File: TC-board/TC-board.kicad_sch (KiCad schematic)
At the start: 7 parts, among them J1 DB15_Female, J3 PCIE-LP-01-01-F-DV-A-TR

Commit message: Updated HX, TC boards.
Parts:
- removed U?: PCF8575_Breakout, symbol PCF8575_Breakout:PCF8575_Breakout
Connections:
- net +3.3V: now also J3.B12, J3.B13
- net GND: now also J3.A11, J3.A14, J3.A3, J3.A7, J3.B11, J3.B14, J3.B8
- net MISO: now also J3.B3
- net SCK: now also J3.B1
- net TC1_CS: now also J3.B9
- net TC2_CS: now also J3.B10
- no-connect marks 22 -> 32
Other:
- note removed: "GPIO Expander"

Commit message: Updated schematics of TC,PT
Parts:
- removed J?: Conn_01x06_Male, symbol Connector:Conn_01x06_Male
- added J3: Conn_01x08_Male, Connector_PinHeader_2.54mm:PinHeader_1x08_P2.54mm_Vertical, symbol Connector:Conn_01x08_Male
- added JP1, JP2, JP3: SolderJumper_3_Open, Jumper:SolderJumper-3_P2.0mm_Open_TrianglePad1.0x1.5mm, symbol Jumper:SolderJumper_3_Open
- added JP4: SolderJumper_2_Open, Jumper:SolderJumper-2_P1.3mm_Open_TrianglePad1.0x1.5mm, symbol Jumper:SolderJumper_2_Open
- added U4: MAX31855KASA, MAX31855_Breakout:MAX31855_Breakout, symbol Sensor_Temperature:MAX31855KASA
- U1, U2, U3: renamed from U?; footprint Package_SO:SOIC-8_3.9x4.9mm_P1.27mm -> MAX31855_Breakout:MAX31855_Breakout
- renumbered J3 to J2
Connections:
- net +3.3V: now also J2.B14, U4.4 (VCC); no longer J2.B12
- net GND: now also J2.A12, J2.A15, J2.A6, J2.B12, J2.B15, J2.B3, U4.1 (GND); no longer J2.A11, J2.A14, J2.A7, J2.B11, J2.B14
- net TC1_CS: now also JP1.1 (A); no longer J2.B9
- net TC1_T+: now also J3.2 (Pin_2)
- net TC1_T-: now also J3.1 (Pin_1)
- net TC2_CS: now also JP2.1 (A); no longer J2.B10
- net TC2_T+: now also J3.4 (Pin_4)
- net TC2_T-: now also J3.3 (Pin_3)
- net TC3_CS: now also JP3.1 (A)
- net TC3_T+: now also J3.6 (Pin_6)
- net TC3_T-: now also J3.5 (Pin_5)
- net SPI1_SCK: now reaches J2.A4
- net SPI1_SCK: now also U1.5 (SCK), U2.5 (SCK), U3.5 (SCK)
- net SPI1_MISO: now reaches J2.A5
- net SPI1_MISO: now also U1.7 (SO), U2.7 (SO), U3.7 (SO)
- net SPI0_MISO: now reaches J2.B2
- net SPI0_MISO: now also U4.7 (SO)
- net TC4_T+: now reaches J1.12 (P12)
- net TC4_T+: now also J3.8 (Pin_8), U4.3 (T+)
- net TC4_T-: now reaches J1.4
- net TC4_T-: now also J3.7 (Pin_7), U4.2 (T-)
- removed net MISO: J2.B3, U1.7 (SO), U2.7 (SO), U3.7 (SO)
- removed net SCK: J2.B1, U1.5 (SCK), U2.5 (SCK), U3.5 (SCK)
- new net CS1: J2.B9, JP1.2 (C)
- new net CS2: J2.B10, JP2.2 (C)
- new net CS3: J2.B11, JP3.2 (C)
- new net CS4: J2.A11, JP4.2 (B)
- new net SPI0_SCK: J2.B1, U4.5 (SCK)
- new net TC4_CS: JP1.3 (B), JP2.3 (B), JP3.3 (B), JP4.1 (A), U4.6 (~{CS})
- no-connect marks 32 -> 25
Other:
- moved on the sheet: U1, U2, U3

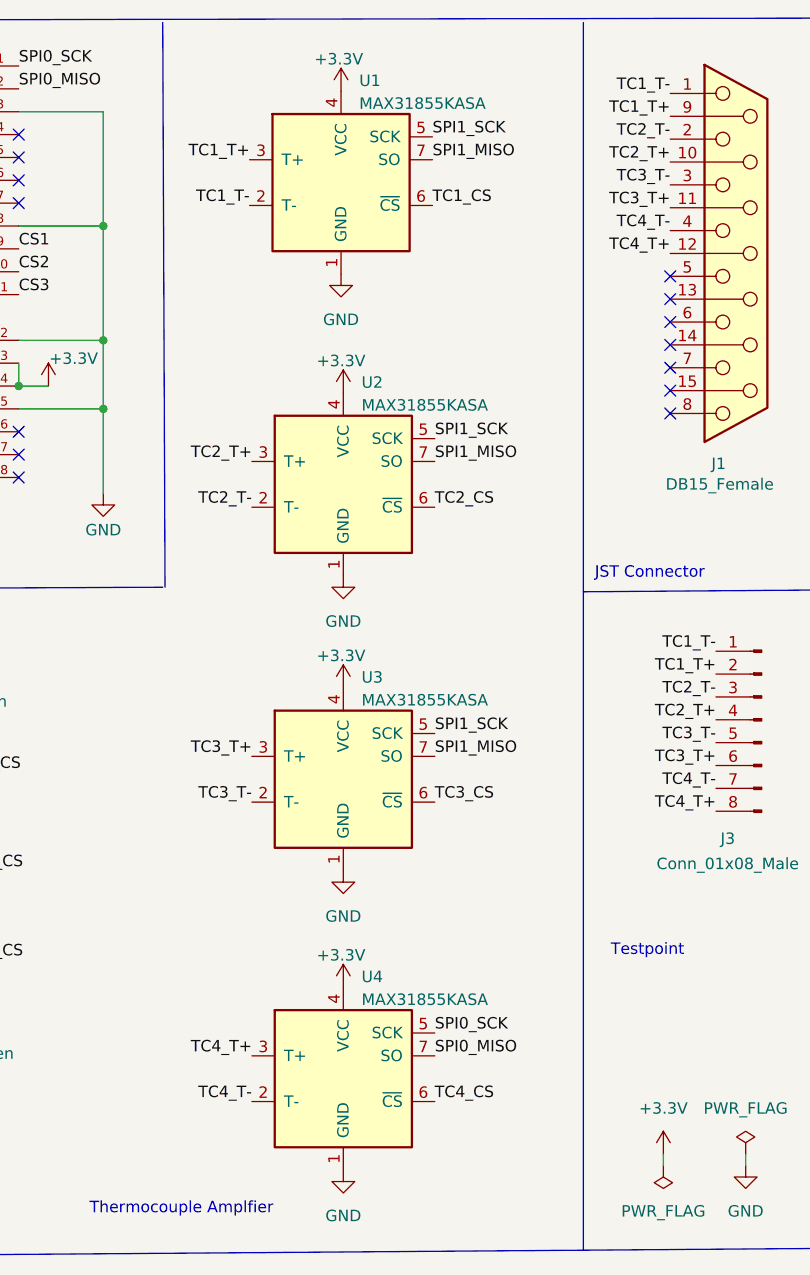
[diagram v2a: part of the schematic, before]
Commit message: Replaced mosfet board with Conor's design using BTS3080EJXUMA1. Modified max31855 symbol to have A (separate assembly) reference designator.
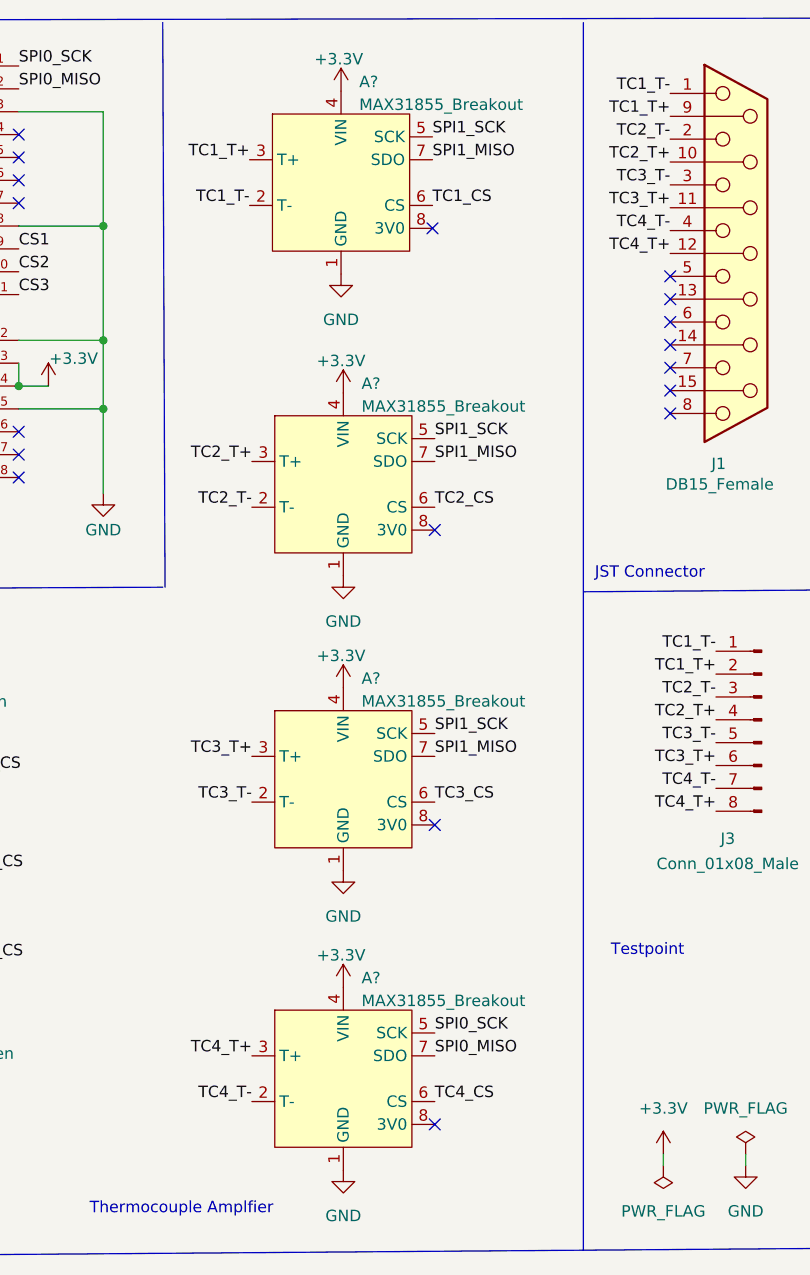
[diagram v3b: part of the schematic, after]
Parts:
- removed U1, U2, U3, U4: MAX31855KASA, MAX31855_Breakout:MAX31855_Breakout, symbol Sensor_Temperature:MAX31855KASA
- added A? (x4): MAX31855_Breakout, symbol MAX31855_Breakout:MAX31855_Breakout
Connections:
- net +3.3V: now also A?.4 (VIN), A?.4 (VIN), A?.4 (VIN), A?.4 (VIN)
- net GND: now also A?.1 (GND), A?.1 (GND), A?.1 (GND), A?.1 (GND)
- net SPI0_MISO: now also A?.7 (SDO)
- net SPI0_SCK: now also A?.5 (SCK)
- net SPI1_MISO: now also A?.7 (SDO), A?.7 (SDO), A?.7 (SDO)
- net SPI1_SCK: now also A?.5 (SCK), A?.5 (SCK), A?.5 (SCK)
- net TC1_CS: now also A?.6 (CS)
- net TC1_T+: now also A?.3 (T+)
- net TC1_T-: now also A?.2 (T-)
- net TC2_CS: now also A?.6 (CS)
- net TC2_T+: now also A?.3 (T+)
- net TC2_T-: now also A?.2 (T-)
- net TC3_CS: now also A?.6 (CS)
- net TC3_T+: now also A?.3 (T+)
- net TC3_T-: now also A?.2 (T-)
- net TC4_CS: now also A?.6 (CS)
- net TC4_T+: now also A?.3 (T+)
- net TC4_T-: now also A?.2 (T-)
- no-connect marks 25 -> 29

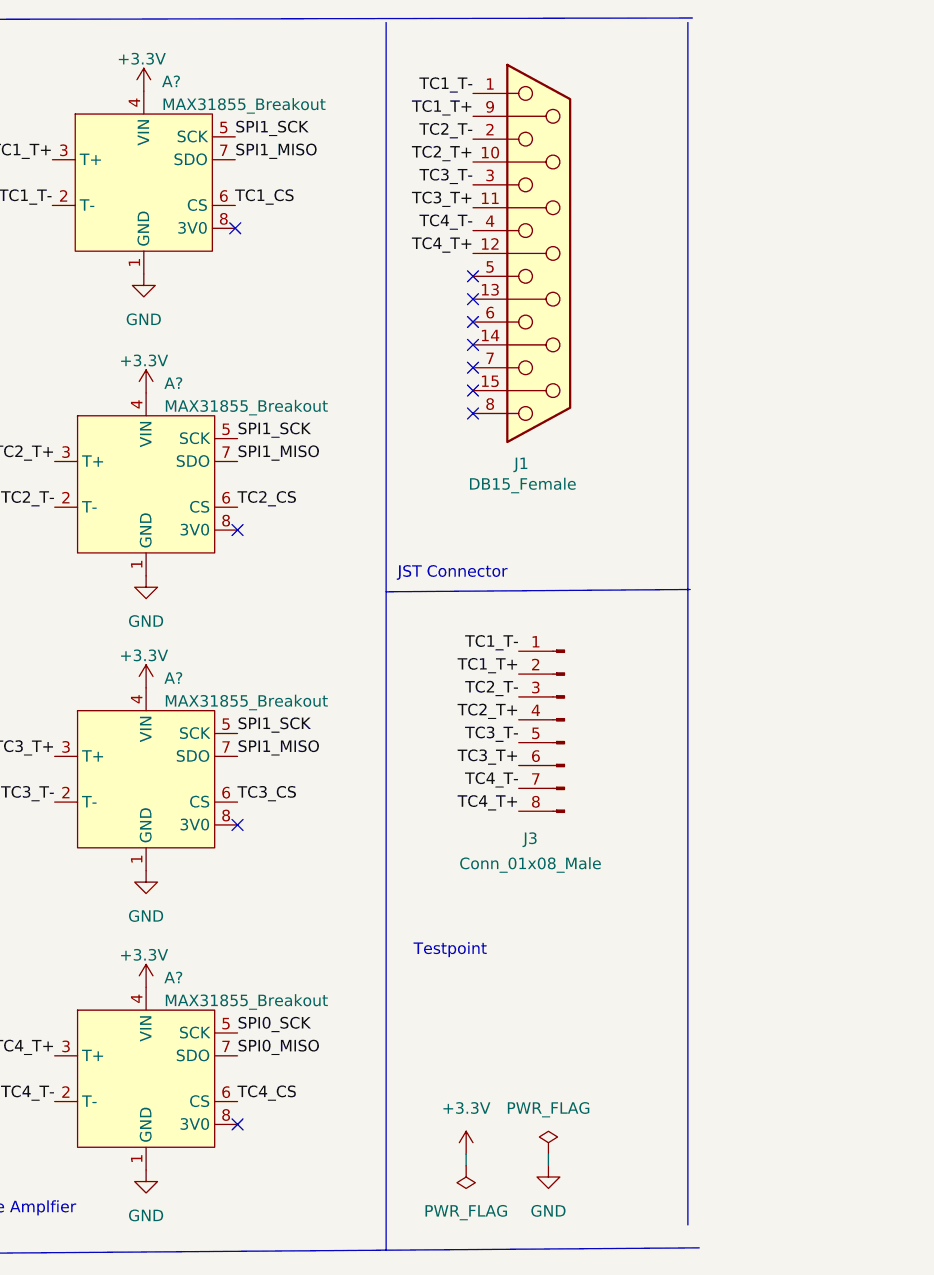
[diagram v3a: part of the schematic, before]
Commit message: Updated HX, TC, and MOSFET board.
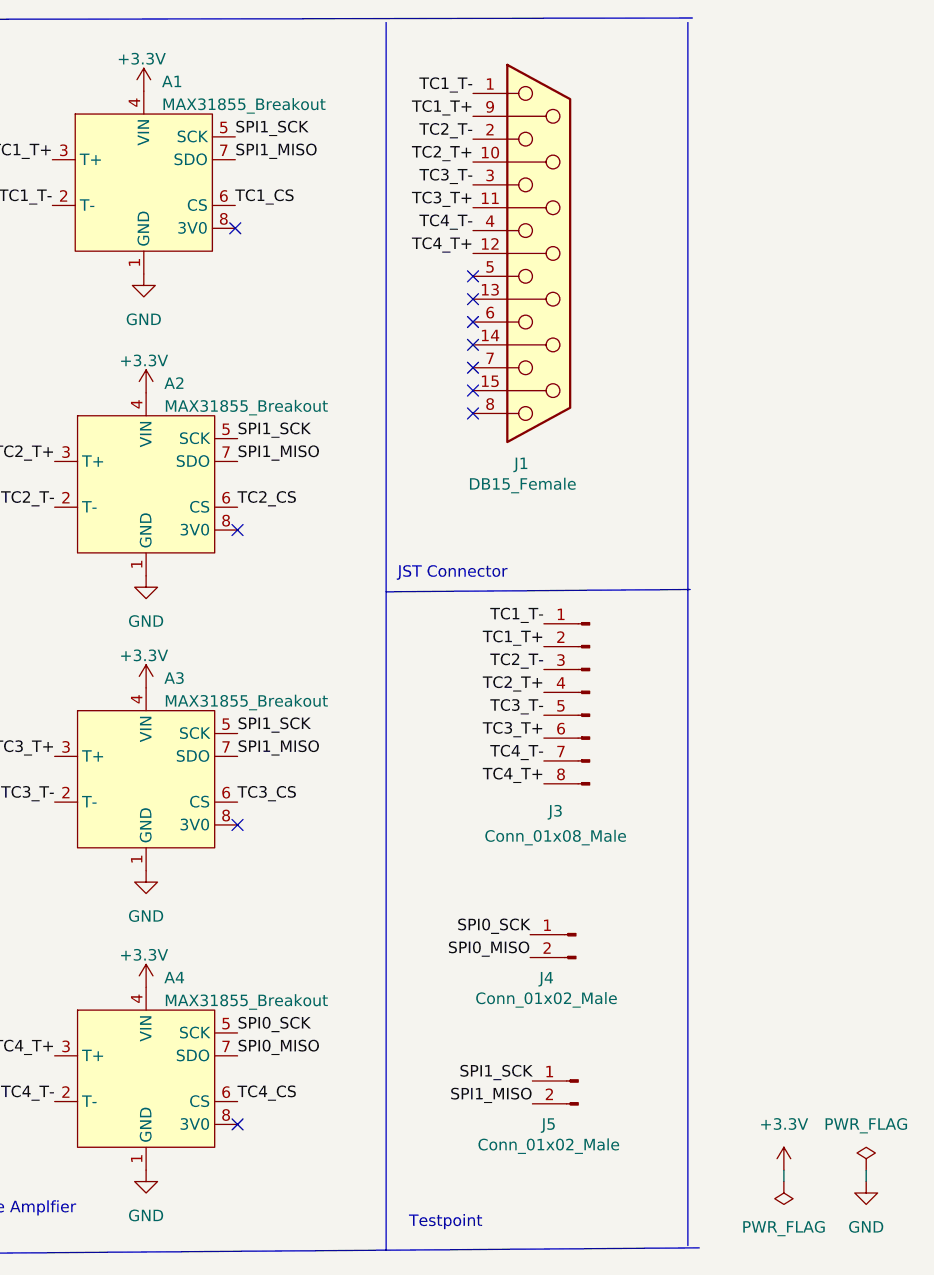
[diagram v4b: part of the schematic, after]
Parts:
- added J4, J5: Conn_01x02_Male, Connector_PinHeader_1.27mm:PinHeader_1x02_P1.27mm_Vertical, symbol Connector:Conn_01x02_Male
- A1, A2, A3, A4: renamed from A?; footprint (none) -> MAX31855_Breakout:MAX31855_Breakout
- J2: footprint PCIe_x1_card_edge:PCIe_x1_card_edge -> Connector_PCBEdge:BUS_PCIexpress_x1
- J3: footprint Connector_PinHeader_2.54mm:PinHeader_1x08_P2.54mm_Vertical -> Connector_PinHeader_1.27mm:PinHeader_1x08_P1.27mm_Vertical
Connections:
- net SPI0_MISO: now also J4.2 (Pin_2)
- net SPI0_SCK: now also J4.1 (Pin_1)
- net SPI1_MISO: now also J5.2 (Pin_2)
- net SPI1_SCK: now also J5.1 (Pin_1)
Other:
- moved on the sheet: J3

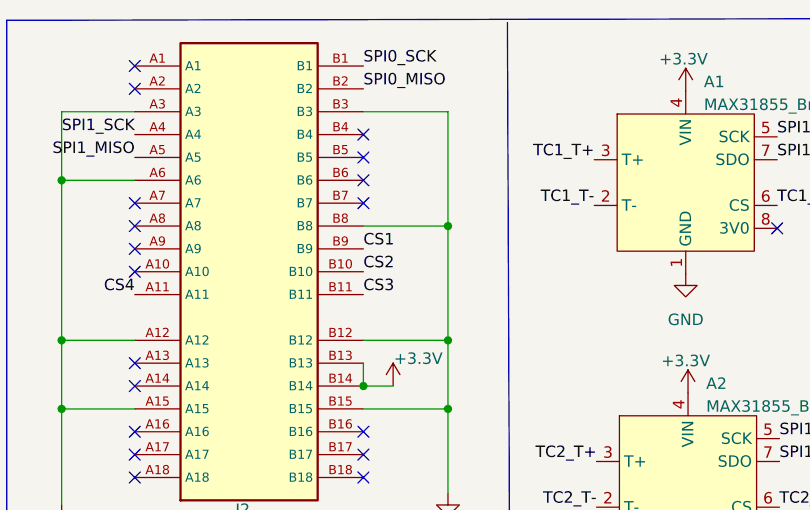
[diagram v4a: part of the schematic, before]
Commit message: Updated pcie and fixed HX, MOSFET, TC board. Also added hierarchical sheet.
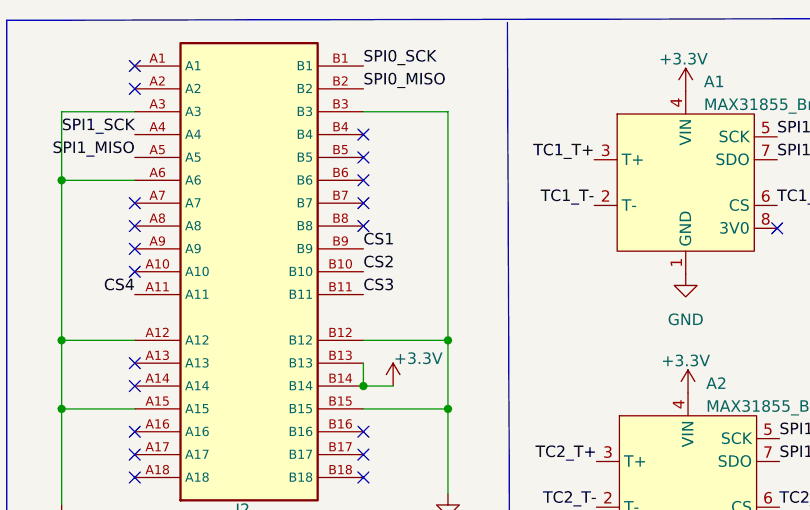
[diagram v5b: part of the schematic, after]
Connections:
- net GND: no longer J2.B8
- no-connect marks 29 -> 30
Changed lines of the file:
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@@
   (junction (at 72.136 46.99) (diameter 0) (color 0 0 0 0)
-  )
-  (junction (at 115.062 52.07) (diameter 0) (color 0 0 0 0)
   )
   (junction (at 72.136 64.77) (diameter 0) (color 0 0 0 0)
@@
   (no_connect (at 105.664 80.01))
   (no_connect (at 105.664 41.91))
+  (no_connect (at 105.664 52.07))
   (no_connect (at 105.664 74.93))
   (no_connect (at 80.264 49.53))
@@
   )
   (polyline (pts (xy 66.04 29.21) (xy 66.04 166.624))
-    (stroke (width 0) (type default) (color 0 0 0 0))
-  )
-  (wire (pts (xy 105.664 52.07) (xy 115.062 52.07))
     (stroke (width 0) (type default) (color 0 0 0 0))
   )
@@
     (stroke (width 0) (type default) (color 0 0 0 0))
   )
-  (wire (pts (xy 115.062 39.37) (xy 115.062 52.07))
+  (wire (pts (xy 115.062 39.37) (xy 115.062 64.77))
     (stroke (width 0) (type default) (color 0 0 0 0))
   )
-  (wire (pts (xy 115.062 52.07) (xy 115.062 64.77))
-    (stroke (width 0) (type default) (color 0 0 0 0))
-  )
